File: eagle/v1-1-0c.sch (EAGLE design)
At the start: 176 parts, among them J1 CR22A-44D-2.54DSA(70), J3 26-60-4040, J4 AUDIO_JACK_3.5MM_PTH, J5 DIN5, SW1 3PDT-AQ-SWITCH, SW2 9077-1, U10 7805, U11 74LS10N, U13 74LS04N, U14 4528N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

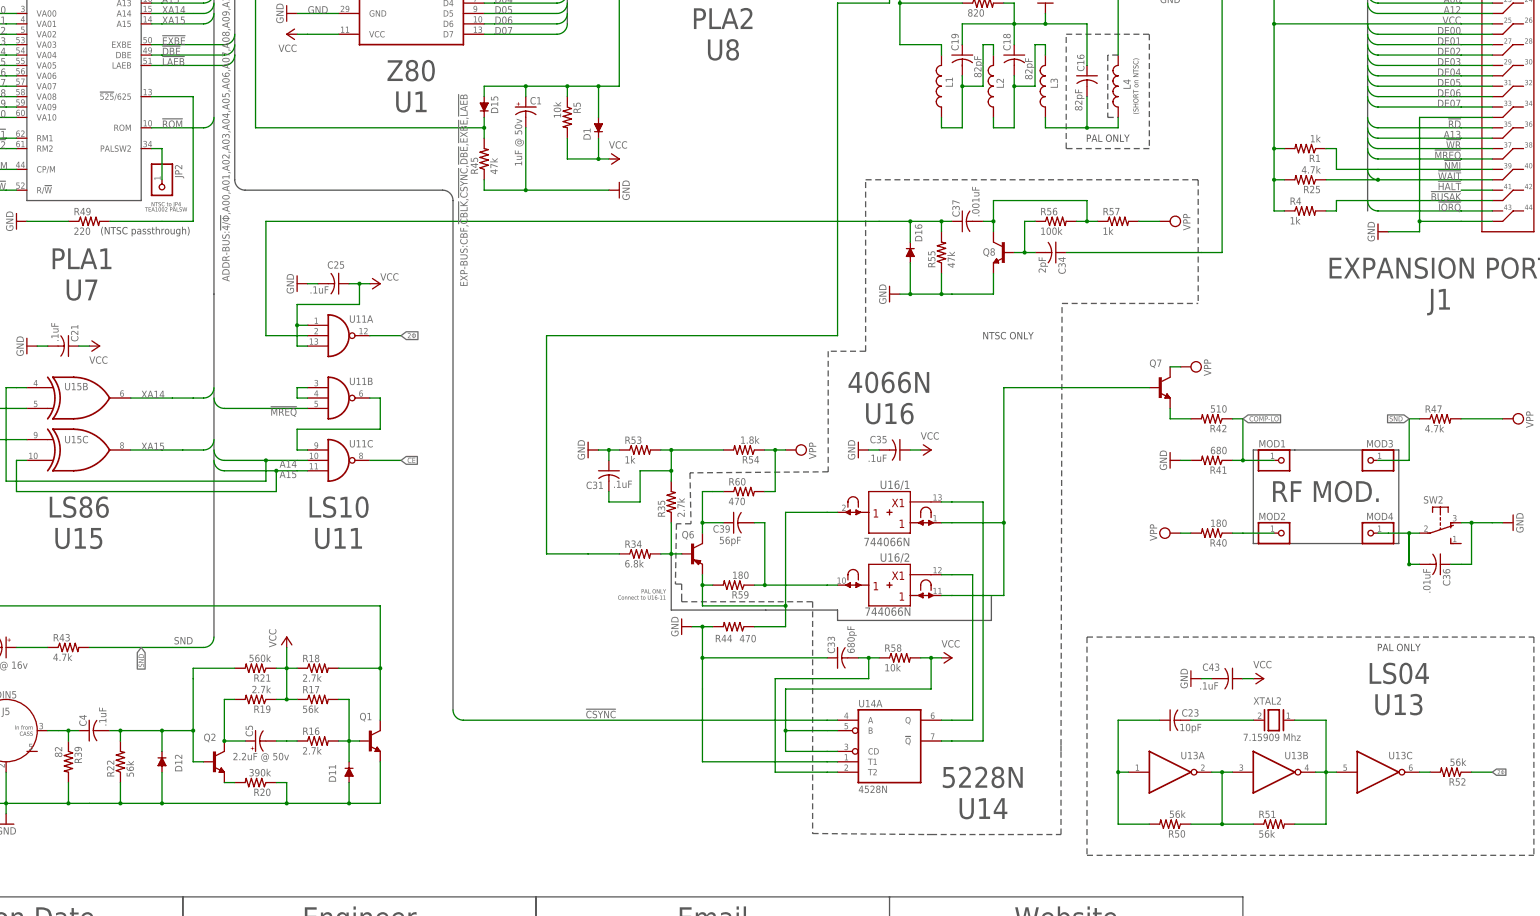
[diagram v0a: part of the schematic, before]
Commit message: Clean up of values from MW input
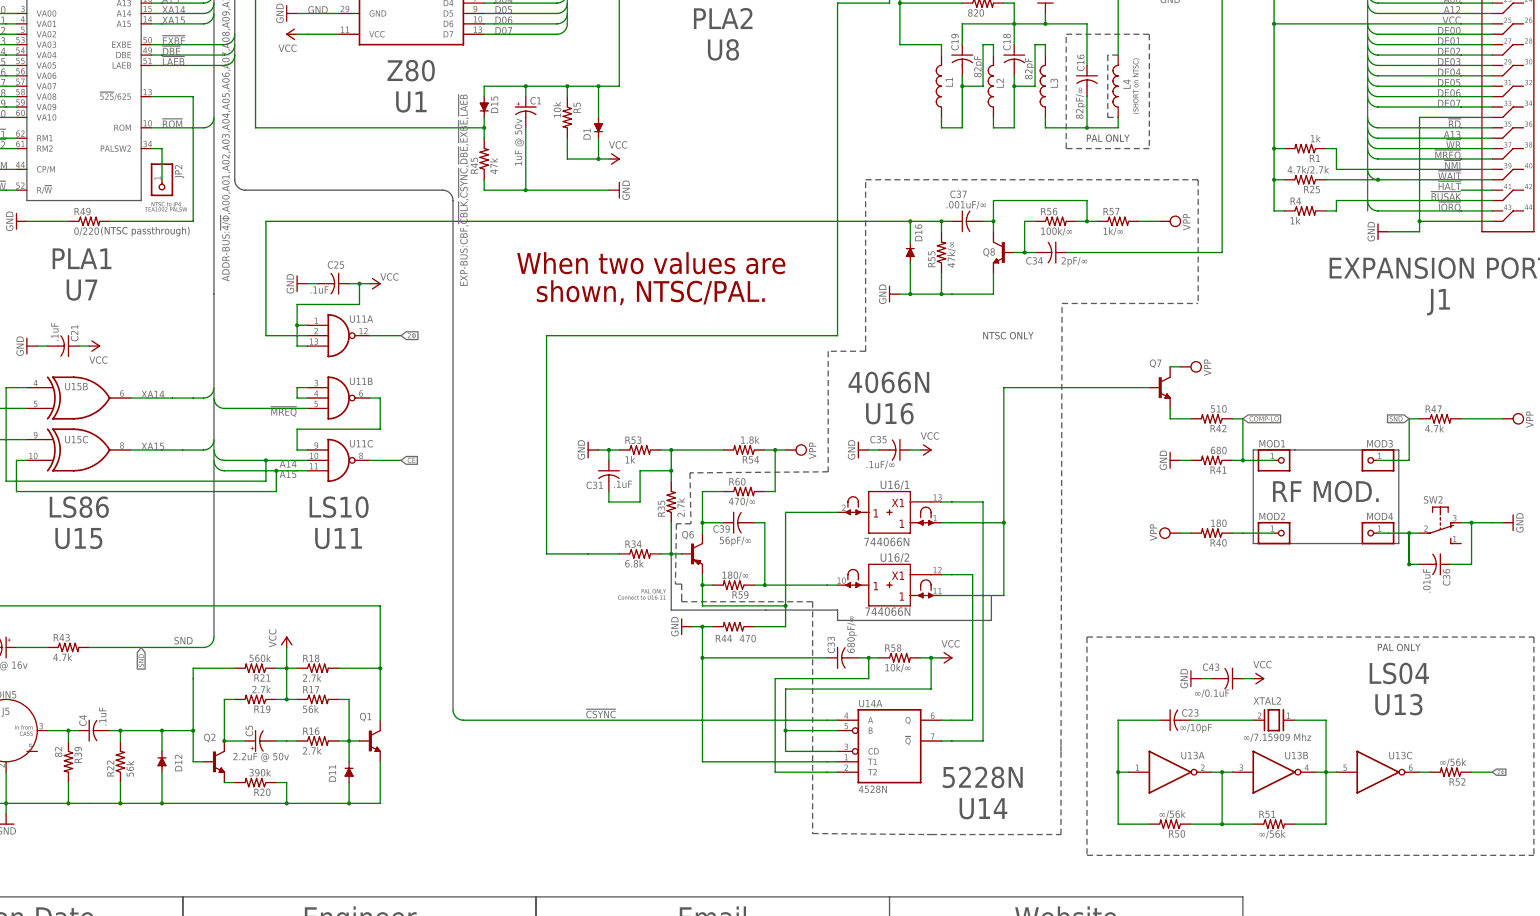
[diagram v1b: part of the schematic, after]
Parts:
- C16: value 82pF -> 82pF/∞
- C23: value 10pF -> ∞/10pF
- C33: value 680pF -> 680pF/∞
- C34: value 2pF -> 2pF/∞
- C35: value .1uF -> .1uF/∞
- C37: value .001uF -> .001uF/∞
- C39: value 56pF -> 56pF/∞
- C43: value .1uF -> ∞/0.1uF
- R25: value 4.7k -> 4.7k/2.7k
- R49: value 220 -> 0/220
- R50, R51, R52: value 56k -> ∞/56k
- R55: value 47k -> 47k/∞
- R56: value 100k -> 100k/∞
- R57: value 1k -> 1k/∞
- R58: value 10k -> 10k/∞
- R59: value 180 -> 180/∞
- R60: value 470 -> 470/∞
- XTAL2: value 7.15909 Mhz -> ∞/7.15909 Mhz
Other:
- note added: "When two values are shown, NTSC/PAL."

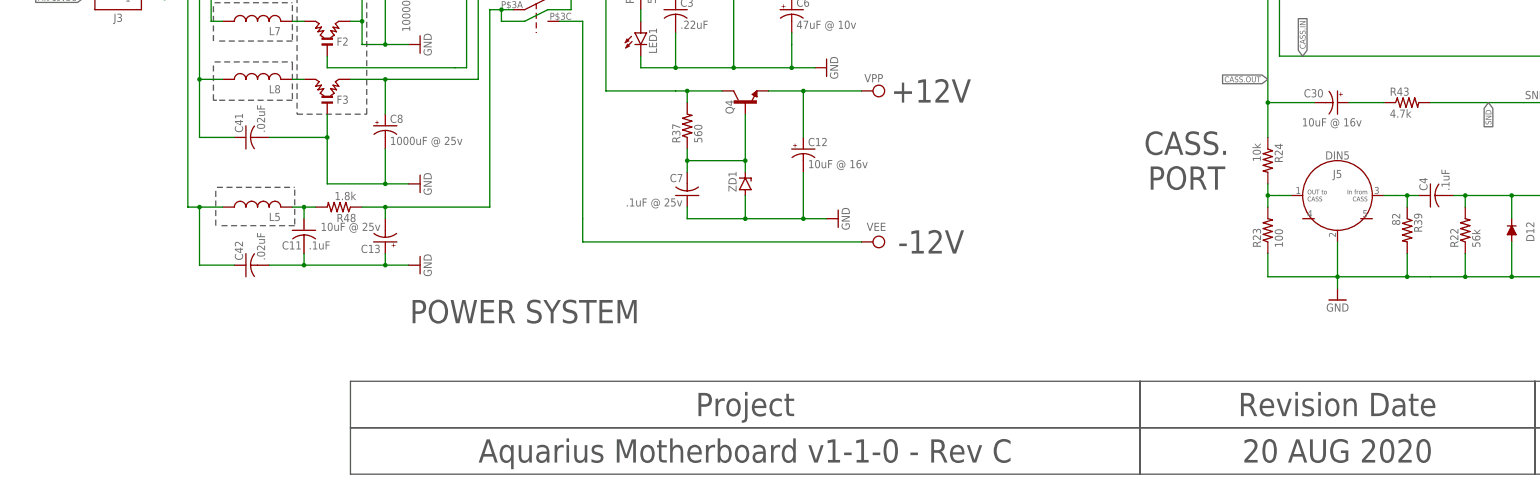
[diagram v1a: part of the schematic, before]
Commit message: Fix gitignore
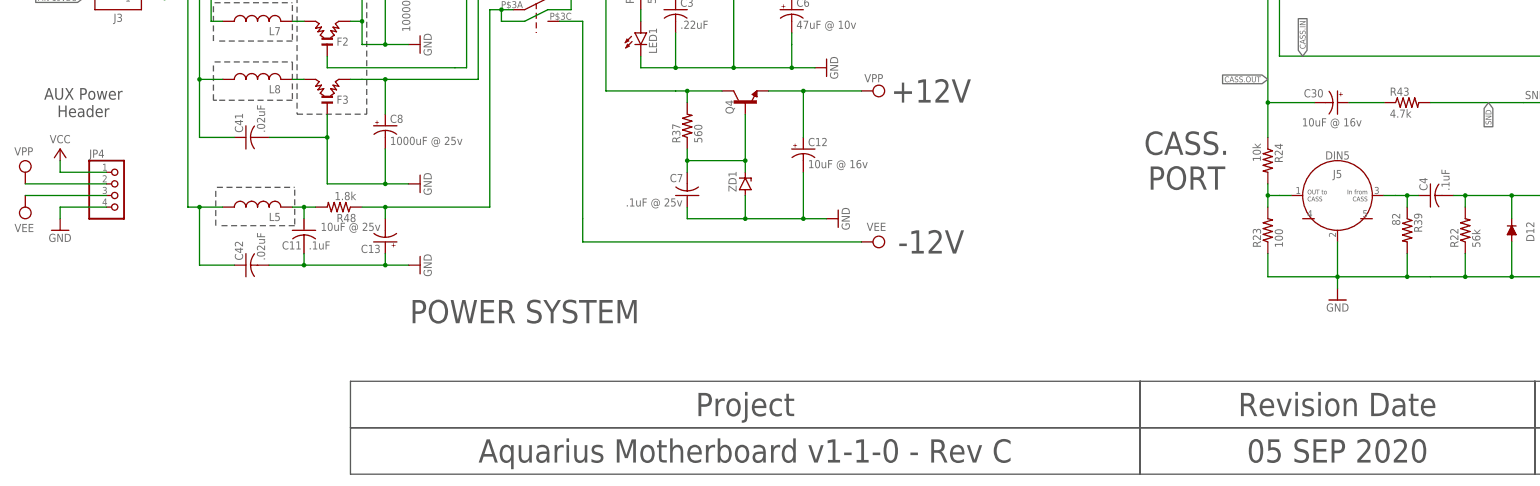
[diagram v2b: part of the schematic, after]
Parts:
- added JP4: (no value), aquarius2:PINHD-1X4
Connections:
- net GND: now also JP4.4
- net VCC: now also JP4.1
- net VEE: now also JP4.3
- net VPP: now also JP4.2
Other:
- note added: "05 SEP 2020"
- note added: "AUX Power Header"
- note removed: "20 AUG 2020"
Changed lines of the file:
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@@
 <part name="GND19" library="supply1" library_urn="urn:adsk.eagle:library:371" deviceset="GND" device=""/>
 <part name="P+8" library="supply1" library_urn="urn:adsk.eagle:library:371" deviceset="VCC" device=""/>
+<part name="JP4" library="aquarius2" deviceset="PINHD-1X4" device="" package3d_urn="urn:adsk.eagle:package:22407/2"/>
+<part name="GND34" library="supply1" library_urn="urn:adsk.eagle:library:371" deviceset="GND" device=""/>
+<part name="P+15" library="supply1" library_urn="urn:adsk.eagle:library:371" deviceset="VCC" device=""/>
+<part name="SUPPLY7" library="supply2" library_urn="urn:adsk.eagle:library:372" deviceset="VPP" device=""/>
+<part name="SUPPLY12" library="supply2" library_urn="urn:adsk.eagle:library:372" deviceset="VEE" device=""/>
 </parts>
 <sheets>
@@
 <wire x1="261.62" y1="15.24" x2="261.62" y2="5.08" width="0.1524" layer="97"/>
 <wire x1="261.62" y1="5.08" x2="347.98" y2="5.08" width="0.1524" layer="97"/>
-<text x="304.8" y="7.62" size="5.08" layer="97" align="bottom-center">20 AUG 2020</text>
+<text x="304.8" y="7.62" size="5.08" layer="97" align="bottom-center">05 SEP 2020</text>
 <wire x1="347.98" y1="15.24" x2="347.98" y2="25.4" width="0.1524" layer="97"/>
 <wire x1="347.98" y1="25.4" x2="261.62" y2="25.4" width="0.1524" layer="97"/>
@@
 <text x="462.534" y="176.784" size="5.08" layer="94" distance="35" align="center">When two values are
 shown, NTSC/PAL.</text>
+<text x="30.48" y="86.36" size="2.54" layer="97" align="center">AUX Power
+Header</text>
 </plain>
 <instances>
@@
 <attribute name="VALUE" x="609.6" y="81.28" size="1.778" layer="96"/>
 </instance>
+<instance part="JP4" gate="A" x="38.1" y="66.04" smashed="yes">
+<attribute name="NAME" x="31.75" y="74.295" size="1.778" layer="95"/>
+<attribute name="VALUE" x="31.75" y="58.42" size="1.778" layer="96"/>
+</instance>
+<instance part="GND34" gate="1" x="25.4" y="58.42" smashed="yes">
+<attribute name="VALUE" x="22.86" y="55.88" size="1.778" layer="96"/>
+</instance>
+<instance part="P+15" gate="VCC" x="25.4" y="76.2" smashed="yes">
+<attribute name="VALUE" x="23.114" y="77.47" size="1.778" layer="96"/>
+</instance>
+<instance part="SUPPLY7" gate="G$1" x="17.78" y="71.12" smashed="yes">
+<attribute name="VALUE" x="15.367" y="74.803" size="1.778" layer="96"/>
+</instance>
+<instance part="SUPPLY12" gate="G$1" x="17.78" y="63.5" smashed="yes" rot="R180">
+<attribute name="VALUE" x="19.685" y="59.817" size="1.778" layer="96" rot="R180"/>
+</instance>
 </instances>
 <busses>
@@
 <pinref part="GND19" gate="1" pin="GND"/>
 </segment>
+<segment>
+<pinref part="JP4" gate="A" pin="4"/>
+<wire x1="35.56" y1="63.5" x2="25.4" y2="63.5" width="0.1524" layer="91"/>
+<pinref part="GND34" gate="1" pin="GND"/>
+<wire x1="25.4" y1="63.5" x2="25.4" y2="60.96" width="0.1524" layer="91"/>
+</segment>
 </net>
 <net name="N$175" class="0">
@@
 <pinref part="P+8" gate="VCC" pin="VCC"/>
 </segment>
+<segment>
+<pinref part="JP4" gate="A" pin="1"/>
+<wire x1="35.56" y1="71.12" x2="25.4" y2="71.12" width="0.1524" layer="91"/>
+<pinref part="P+15" gate="VCC" pin="VCC"/>
+<wire x1="25.4" y1="71.12" x2="25.4" y2="73.66" width="0.1524" layer="91"/>
+</segment>
 </net>
 <net name="N$767" class="0">
@@
 <wire x1="139.7" y1="55.88" x2="200.66" y2="55.88" width="0.1524" layer="91"/>
 </segment>
+<segment>
+<pinref part="JP4" gate="A" pin="3"/>
+<pinref part="SUPPLY12" gate="G$1" pin="VEE"/>
+<wire x1="35.56" y1="66.04" x2="17.78" y2="66.04" width="0.1524" layer="91"/>
+</segment>
 </net>
 <net name="N$651" class="0">
@@
 <junction x="596.9" y="266.7"/>
 </segment>
+<segment>
+<pinref part="JP4" gate="A" pin="2"/>
+<pinref part="SUPPLY7" gate="G$1" pin="VPP"/>
+<wire x1="35.56" y1="68.58" x2="17.78" y2="68.58" width="0.1524" layer="91"/>
+</segment>
 </net>

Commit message: Updates
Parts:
- J2: device aquarius2:PINHD-1X16 -> aquarius2:PINHD-1X17
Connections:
- net GND: now also J2.17

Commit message: Updates
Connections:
- net VCC: now also U5.21
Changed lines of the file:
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@@
 <segment>
 <pinref part="U5" gate="G$1" pin="24"/>
-<wire x1="195.58" y1="302.26" x2="198.12" y2="302.26" width="0.1524" layer="91"/>
+<wire x1="195.58" y1="302.26" x2="196.85" y2="302.26" width="0.1524" layer="91"/>
 <label x="198.12" y="302.26" size="1.778" layer="95"/>
+<pinref part="U5" gate="G$1" pin="21"/>
+<wire x1="195.58" y1="294.64" x2="196.85" y2="294.64" width="0.1524" layer="91"/>
+<wire x1="196.85" y1="294.64" x2="196.85" y2="302.26" width="0.1524" layer="91"/>
+<wire x1="196.85" y1="302.26" x2="198.12" y2="302.26" width="0.1524" layer="91"/>
+<junction x="196.85" y="302.26"/>
 </segment>
 <segment>
